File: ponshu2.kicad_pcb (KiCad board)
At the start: 2 copper layers, 22 parts, among them J1 Conn_01x02, J2 Conn_01x03, J3 Conn_01x05, SW1 TS-1187A-B-A-B, SW2 TS-1187A-B-A-B, U1 STM32F072CBT6, U2 XC6206P332MR

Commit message: sukoshi susumeta
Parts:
- added J4: Conn_01x02, Connector_PinHeader_2.54mm:PinHeader_1x02_P2.54mm_Vertical, F.Cu at (92.2, 89.4)
- added J5: Conn_01x03, Connector_PinHeader_2.54mm:PinHeader_1x03_P2.54mm_Vertical, F.Cu at (83.6, 91.2)
- ESD1, ESD2: footprint Diode_SMD:D_SOD-882 -> Diode_SMD:D_0402_1005Metric
- SW1, SW2: footprint random-keyboard-parts:SKQG-1155865 -> random-keyboard-parts:SKQGADE010
- U2: footprint Package_TO_SOT_SMD:SOT-23-3 -> Package_TO_SOT_SMD:SOT-23
- USB1: footprint Connector_USB:USB_C_Receptacle_HRO_TYPE-C-31-M-12 -> Type-C:HRO-TYPE-C-31-M-12-HandSoldering
- moved R2 24.6 mm to (69.3, 79.6), turned to -90 degrees
- moved J3 17.3 mm to (104.4, 70.6)
- moved R3 16.1 mm to (69.3, 74.0), turned to 90 degrees
- moved ESD1 2.62 mm to (70.9, 75.5), turned to -90 degrees
- moved ESD2 2.51 mm to (70.9, 78.0), turned to 90 degrees
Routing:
- net D+: track 0.00 -> 9.99 mm
- net Net-(F1-Pad1): track 0.00 -> 9.76 mm, vias 0 -> 2
- net GND: track 0.00 -> 8.76 mm
- net D-: track 0.00 -> 8.25 mm
- net Net-(USB1-CC1): track 0.00 -> 4.49 mm
- net Net-(USB1-CC2): track 0.00 -> 4.33 mm

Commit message: kiban susumeta
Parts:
- added J1: Conn_01x04, Connector_PinHeader_2.54mm:PinHeader_1x04_P2.54mm_Vertical, F.Cu at (82.9, 80.5)
- added J2: Conn_01x01, Connector_PinHeader_2.54mm:PinHeader_1x01_P2.54mm_Vertical, F.Cu at (75.7, 73.3)
- added J6: Conn_01x01, Connector_PinHeader_2.54mm:PinHeader_1x01_P2.54mm_Vertical, F.Cu at (75.7, 80.3)
- C1: renamed from C7; moved to B.Cu
- C2: renamed from C8; moved to B.Cu
- F1: moved to B.Cu
- J3: value Conn_01x05 -> Conn_01x01; footprint Connector_PinHeader_2.54mm:PinHeader_1x05_P2.54mm_Vertical -> Connector_PinHeader_2.54mm:PinHeader_1x01_P2.54mm_Vertical
- J4: value Conn_01x02 -> Conn_01x01; footprint Connector_PinHeader_2.54mm:PinHeader_1x02_P2.54mm_Vertical -> Connector_PinHeader_2.54mm:PinHeader_1x01_P2.54mm_Vertical
- J5: value Conn_01x03 -> Conn_01x01; footprint Connector_PinHeader_2.54mm:PinHeader_1x03_P2.54mm_Vertical -> Connector_PinHeader_2.54mm:PinHeader_1x01_P2.54mm_Vertical
- U1: renamed from U2; moved to B.Cu
- moved U2 39.8 mm to (94.5, 75.7), turned to 180 degrees
- moved C5 38.9 mm to (91.4, 69.3)
- moved SW2 38.6 mm to (82.5, 96.5)
- moved J3 33.3 mm to (72.5, 80.3)
- moved R3 32.9 mm to (106.6, 92.4)
- moved C8 29.5 mm to (88.1, 79.0), turned to 90 degrees
- moved C7 27.5 mm to (100.8, 74.5), turned to -90 degrees
- moved C3 22.9 mm to (80.8, 101.9)
- moved J4 21.5 mm to (75.7, 75.6)
- moved U1 19.9 mm to (72.5, 74.6), turned to 90 degrees
- moved SW1 19.7 mm to (100.0, 97.0)
- moved C6 18.2 mm to (97.6, 82.0), turned to 180 degrees
- moved J5 15.5 mm to (75.7, 77.9)
- moved C1 15.1 mm to (69.1, 73.8), turned to -90 degrees
- moved C4 14.4 mm to (100.8, 79.0), turned to -90 degrees
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- renumbered C6 to C3, C5 to C4, C4 to C5, C3 to C6, C2 to C7, C1 to C8, J1 to J7, J2 to J8, R2 to R1, R3 to R2, R1 to R3, SW2 to SW1, SW1 to SW2, U1 to U2
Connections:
- J3 pad 1: GND -> +3.3V
- J4 pad 1: +5v -> D-
- J5 pad 1: D- -> D+
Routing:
- net GND: track 8.76 -> 119.9 mm, vias 0 -> 6
- net +3.3V: track 0.00 -> 109.2 mm, vias 0 -> 8
- net D+: track 9.99 -> 31.5 mm
- net D-: track 8.25 -> 28.8 mm
- net +5v: track 0.00 -> 11.6 mm, vias 0 -> 1
- net Net-(F1-Pad1): track 9.76 -> 12.6 mm
- added copper zone on B.Cu, net GND
- added copper zone on F.Cu, net GND
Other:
- board outline added: 61.6 x 41.7 mm
- board text added: "+"
- board text added: "-"
- board text added: "3"
- board text added: "3V"
- board text added: "5V"
- board text added: "D+"
- board text added: "D-"
- board text added: "G"
- board text added: "GD"

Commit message: kiban susumetazo!
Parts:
- added J10: Conn_01x01, Connector_PinHeader_2.54mm:PinHeader_1x01_P2.54mm_Vertical, F.Cu at (92.1, 65.7)
- added J11: Conn_01x01, Connector_PinHeader_2.54mm:PinHeader_1x01_P2.54mm_Vertical, F.Cu at (91.2, 63.4)
- added J12: Conn_01x01, Connector_PinHeader_2.54mm:PinHeader_1x01_P2.54mm_Vertical, F.Cu at (89.5, 65.4)
- added J13: Conn_01x01, Connector_PinHeader_2.54mm:PinHeader_1x01_P2.54mm_Vertical, F.Cu at (91.6, 86.1)
- added J14: Conn_01x01, Connector_PinHeader_2.54mm:PinHeader_1x01_P2.54mm_Vertical, F.Cu at (93.0, 83.8)
- added J15: Conn_01x01, Connector_PinHeader_2.54mm:PinHeader_1x01_P2.54mm_Vertical, F.Cu at (93.9, 86.1)
- added J16: Conn_01x01, Connector_PinHeader_2.54mm:PinHeader_1x01_P2.54mm_Vertical, F.Cu at (95.6, 84.1)
- added J17: Conn_01x01, Connector_PinHeader_2.54mm:PinHeader_1x01_P2.54mm_Vertical, F.Cu at (96.3, 86.2)
- added J18: Conn_01x01, Connector_PinHeader_2.54mm:PinHeader_1x01_P2.54mm_Vertical, F.Cu at (98.2, 83.9)
- added J19: Conn_01x01, Connector_PinHeader_2.54mm:PinHeader_1x01_P2.54mm_Vertical, F.Cu at (99.4, 86.2)
- added J2: Conn_01x01, Connector_PinHeader_2.54mm:PinHeader_1x01_P2.54mm_Vertical, F.Cu at (82.9, 67.2)
- added J20: Conn_01x01, Connector_PinHeader_2.54mm:PinHeader_1x01_P2.54mm_Vertical, F.Cu at (88.5, 63.4)
- added J21: Conn_01x01, Connector_PinHeader_2.54mm:PinHeader_1x01_P2.54mm_Vertical, F.Cu at (87.1, 65.3)
- added J29: Conn_01x01, Connector_PinHeader_2.54mm:PinHeader_1x01_P2.54mm_Vertical, F.Cu at (97.8, 65.8)
- added J3: Conn_01x01, Connector_PinHeader_2.54mm:PinHeader_1x01_P2.54mm_Vertical, F.Cu at (81.5, 65.5)
- added J30: Conn_01x01, Connector_PinHeader_2.54mm:PinHeader_1x01_P2.54mm_Vertical, F.Cu at (96.5, 63.6)
- added J31: Conn_01x01, Connector_PinHeader_2.54mm:PinHeader_1x01_P2.54mm_Vertical, F.Cu at (95.0, 65.7)
- added J32: Conn_01x01, Connector_PinHeader_2.54mm:PinHeader_1x01_P2.54mm_Vertical, F.Cu at (93.7, 63.5)
- added J33: Conn_01x01, Connector_PinHeader_2.54mm:PinHeader_1x01_P2.54mm_Vertical, F.Cu at (90.4, 83.8)
- added J34: Conn_01x01, Connector_PinHeader_2.54mm:PinHeader_1x01_P2.54mm_Vertical, F.Cu at (79.4, 69.3)
- added J35: Conn_01x01, Connector_PinHeader_2.54mm:PinHeader_1x01_P2.54mm_Vertical, F.Cu at (82.2, 84.2)
- added J36: Conn_01x01, Connector_PinHeader_2.54mm:PinHeader_1x01_P2.54mm_Vertical, F.Cu at (84.8, 84.2)
- added J37: Conn_01x01, Connector_PinHeader_2.54mm:PinHeader_1x01_P2.54mm_Vertical, F.Cu at (80.0, 67.3)
- added J38: Conn_01x01, Connector_PinHeader_2.54mm:PinHeader_1x01_P2.54mm_Vertical, F.Cu at (82.2, 86.5)
- added J39: Conn_01x01, Connector_PinHeader_2.54mm:PinHeader_1x01_P2.54mm_Vertical, F.Cu at (81.4, 69.5)
- added J4: Conn_01x01, Connector_PinHeader_2.54mm:PinHeader_1x01_P2.54mm_Vertical, F.Cu at (87.4, 83.9)
- added J5: Conn_01x01, Connector_PinHeader_2.54mm:PinHeader_1x01_P2.54mm_Vertical, F.Cu at (83.8, 65.2)
- added J6: Conn_01x01, Connector_PinHeader_2.54mm:PinHeader_1x01_P2.54mm_Vertical, F.Cu at (89.2, 86.4)
- added J7: Conn_01x01, Connector_PinHeader_2.54mm:PinHeader_1x01_P2.54mm_Vertical, F.Cu at (86.9, 86.2)
- added J8: Conn_01x01, Connector_PinHeader_2.54mm:PinHeader_1x01_P2.54mm_Vertical, F.Cu at (79.1, 65.3)
- added J9: Conn_01x01, Connector_PinHeader_2.54mm:PinHeader_1x01_P2.54mm_Vertical, F.Cu at (84.5, 86.4)
- moved C3 32.3 mm to (106.8, 82.8)
- moved SW2 30.1 mm to (107.0, 78.9), turned to 180 degrees
- moved SW1 24.6 mm to (107.0, 73.3)
- moved R3 23.0 mm to (106.7, 69.3)
- moved J28 11.9 mm to (116.3, 70.4)
- moved J27 6.38 mm to (116.2, 60.5)
- moved C6 1.71 mm to (98.8, 80.9), turned to -90 degrees
- moved C8 1.35 mm to (89.1, 80.0), turned to 180 degrees
- renumbered J2 to J22, J3 to J23, J4 to J24, J5 to J25, J6 to J26, J7 to J27, J8 to J28
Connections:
- U2 pad 14: unconnected-(U2-PA4-Pad14) -> Net-(J29-Pin_1)
- U2 pad 15: unconnected-(U2-PA5-Pad15) -> Net-(J30-Pin_1)
- U2 pad 16: unconnected-(U2-PA6-Pad16) -> Net-(J31-Pin_1)
- U2 pad 17: unconnected-(U2-PA7-Pad17) -> Net-(J32-Pin_1)
- U2 pad 18: unconnected-(U2-PB0-Pad18) -> Net-(J10-Pin_1)
- U2 pad 19: unconnected-(U2-PB1-Pad19) -> Net-(J11-Pin_1)
- U2 pad 20: unconnected-(U2-PB2-Pad20) -> Net-(J12-Pin_1)
- U2 pad 21: unconnected-(U2-PB10-Pad21) -> Net-(J20-Pin_1)
- U2 pad 22: unconnected-(U2-PB11-Pad22) -> Net-(J21-Pin_1)
- U2 pad 25: unconnected-(U2-PB12-Pad25) -> Net-(J5-Pin_1)
- U2 pad 26: unconnected-(U2-PB13-Pad26) -> Net-(J2-Pin_1)
- U2 pad 27: unconnected-(U2-PB14-Pad27) -> Net-(J3-Pin_1)
- U2 pad 28: unconnected-(U2-PB15-Pad28) -> Net-(J8-Pin_1)
- U2 pad 29: unconnected-(U2-PA8-Pad29) -> Net-(J36-Pin_1)
- U2 pad 30: unconnected-(U2-PA9-Pad30) -> Net-(J38-Pin_1)
- U2 pad 31: unconnected-(U2-PA10-Pad31) -> Net-(J34-Pin_1)
- U2 pad 38: unconnected-(U2-PA15-Pad38) -> Net-(J33-Pin_1)
- U2 pad 39: unconnected-(U2-PB3-Pad39) -> Net-(J13-Pin_1)
- U2 pad 40: unconnected-(U2-PB4-Pad40) -> Net-(J14-Pin_1)
- U2 pad 41: unconnected-(U2-PB5-Pad41) -> Net-(J15-Pin_1)
- U2 pad 42: unconnected-(U2-PB6-Pad42) -> Net-(J16-Pin_1)
- U2 pad 43: unconnected-(U2-PB7-Pad43) -> Net-(J17-Pin_1)
- U2 pad 45: unconnected-(U2-PB8-Pad45) -> Net-(J18-Pin_1)
- U2 pad 46: unconnected-(U2-PB9-Pad46) -> Net-(J19-Pin_1)
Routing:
- net SWDIO: track 0.00 -> 38.8 mm, vias 0 -> 2
- net Net-(U2-BOOT0): track 0.00 -> 32.9 mm, vias 0 -> 2
- net Net-(J2-Pin_1): track 0.00 -> 20.3 mm, vias 0 -> 2
- net Net-(J8-Pin_1): track 0.00 -> 19.5 mm, vias 0 -> 2
- net Net-(J38-Pin_1): track 0.00 -> 19.0 mm, vias 0 -> 2
- net NRST: track 0.00 -> 17.9 mm
- net Net-(J5-Pin_1): track 0.00 -> 17.7 mm, vias 0 -> 2
- net Net-(J3-Pin_1): track 0.00 -> 16.8 mm, vias 0 -> 2
- net Net-(J34-Pin_1): track 0.00 -> 16.0 mm, vias 0 -> 2
- net Net-(J36-Pin_1): track 0.00 -> 15.5 mm, vias 0 -> 2
- net SWCLK: track 0.00 -> 15.1 mm, vias 0 -> 1
- net GND: track 119.9 -> 134.6 mm, vias 6 -> 7
- net +3.3V: track 109.2 -> 119.1 mm
- net Net-(J19-Pin_1): track 0.00 -> 8.38 mm
- net Net-(J17-Pin_1): track 0.00 -> 8.32 mm, vias 0 -> 1
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- removed copper zone on B.Cu, net GND

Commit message: kiban no ana kankaku hiroku shita
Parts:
- added H1: MountingHole, MountingHole:MountingHole_2.5mm, F.Cu at (77.1, 67.3)
- added H2: MountingHole, MountingHole:MountingHole_2.5mm, F.Cu at (113.4, 67.2)
- added H3: MountingHole, MountingHole:MountingHole_2.5mm, F.Cu at (76.8, 85.1)
- added H4: MountingHole, MountingHole:MountingHole_2.5mm, F.Cu at (113.3, 84.8)
- moved J27 48.4 mm to (68.6, 69.1), turned to 90 degrees
- moved J30 11.6 mm to (107.4, 67.4)
- moved J29 11.6 mm to (109.3, 65.7)
- moved J31 10.7 mm to (105.7, 65.8)
- moved J32 10.5 mm to (103.5, 67.4)
- moved J10 9.91 mm to (102.0, 65.7)
- moved J11 9.72 mm to (100.1, 67.3)
- moved J12 8.77 mm to (98.3, 65.8)
- moved J28 8.57 mm to (114.0, 78.6), turned to 180 degrees
- moved J5 7.98 mm to (91.6, 67.1)
- moved J20 7.83 mm to (96.0, 65.7)
- moved J8 7.25 mm to (86.4, 65.7)
- moved J3 6.91 mm to (88.1, 67.6)
- moved J2 6.90 mm to (89.7, 65.7)
- moved J21 6.36 mm to (93.5, 65.7)
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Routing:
- net Net-(J29-Pin_1): track 1.76 -> 18.3 mm, vias 0 -> 1
- net Net-(J30-Pin_1): track 1.91 -> 14.7 mm, vias 0 -> 1
- net Net-(J31-Pin_1): track 1.91 -> 14.2 mm
- net GND: track 134.6 -> 145.2 mm
- net Net-(J38-Pin_1): track 19.0 -> 29.4 mm
- net Net-(J10-Pin_1): track 2.69 -> 12.4 mm, vias 0 -> 1
- net Net-(J32-Pin_1): track 2.05 -> 11.6 mm
- net Net-(J34-Pin_1): track 16.0 -> 25.3 mm
- net Net-(J8-Pin_1): track 19.5 -> 27.5 mm
- net Net-(J36-Pin_1): track 15.5 -> 23.3 mm
- net +3.3V: track 119.1 -> 126.2 mm
- net Net-(J11-Pin_1): track 2.69 -> 9.24 mm
- net Net-(J12-Pin_1): track 2.68 -> 8.82 mm
- net Net-(J2-Pin_1): track 20.3 -> 26.4 mm
- net Net-(J5-Pin_1): track 17.7 -> 23.4 mm
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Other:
- board size 61.6 x 41.7 mm -> 63.5 x 24.4 mm

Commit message: kiban hobo kansei shita
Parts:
- added REF**: MountingHole_2.1mm, MountingHole:MountingHole_2.1mm, F.Cu at (73.5, 81.5)
- added REF**: MountingHole_2.1mm, MountingHole:MountingHole_2.1mm, F.Cu at (73.5, 71.8)
- added REF**: MountingHole_2.1mm, MountingHole:MountingHole_2.1mm, F.Cu at (73.5, 77.5)
- added REF**: MountingHole_2.1mm, MountingHole:MountingHole_2.1mm, F.Cu at (73.5, 74.2)
- added REF**: MountingHole_2.1mm, MountingHole:MountingHole_2.1mm, F.Cu at (73.5, 75.8)
- added REF**: MountingHole_2.1mm, MountingHole:MountingHole_2.1mm, F.Cu at (73.5, 79.2)
- added REF**: MountingHole_2.1mm, MountingHole:MountingHole_2.1mm, F.Cu at (73.5, 74.9)
- added REF**: MountingHole_2.1mm, MountingHole:MountingHole_2.1mm, F.Cu at (73.5, 78.4)
- added REF**: MountingHole_2.1mm, MountingHole:MountingHole_2.1mm, F.Cu at (73.5, 80.3)
- added REF**: MountingHole_2.1mm, MountingHole:MountingHole_2.1mm, F.Cu at (73.5, 73.4)
- added REF**: MountingHole_2.1mm, MountingHole:MountingHole_2.1mm, F.Cu at (73.5, 72.8)
- moved J27 10.1 mm to (77.1, 74.5), turned to 180 degrees
- moved J19 9.92 mm to (109.3, 86.7)
- moved J17 9.79 mm to (106.0, 86.7)
- moved J18 9.56 mm to (107.7, 84.7)
- moved J16 8.19 mm to (103.8, 85.1)
- moved J15 8.16 mm to (102.0, 86.9)
- moved J14 7.15 mm to (99.9, 85.3)
- moved J13 6.79 mm to (98.3, 87.0)
- moved J33 6.25 mm to (95.9, 86.9)
- moved J7 2.71 mm to (89.5, 86.7)
- moved J6 2.56 mm to (91.4, 85.2)
- moved J9 1.97 mm to (86.4, 86.9)
- moved J4 1.27 mm to (88.1, 85.0)
- moved J38 1.09 mm to (83.2, 86.9)
- moved J36 0.65 mm to (84.7, 84.8)
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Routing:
- net SWDIO: track 39.1 -> 67.4 mm, vias 2 -> 4
- net SWCLK: track 13.0 -> 29.4 mm, vias 1 -> 2
- net GND: track 145.2 -> 160.0 mm, vias 7 -> 9
- net D+: track 36.8 -> 24.3 mm
- net D-: track 34.0 -> 21.5 mm
- net Net-(J19-Pin_1): track 8.38 -> 19.7 mm, vias 0 -> 1
- net Net-(J18-Pin_1): track 5.11 -> 14.9 mm
- net Net-(J16-Pin_1): track 4.95 -> 14.3 mm
- net Net-(J17-Pin_1): track 8.32 -> 17.5 mm
- net Net-(J15-Pin_1): track 6.61 -> 14.0 mm
- net Net-(J14-Pin_1): track 4.08 -> 11.2 mm
- net Net-(J33-Pin_1): track 4.72 -> 9.45 mm
- net NRST: track 17.9 -> 22.5 mm
- net Net-(J13-Pin_1): track 6.74 -> 11.3 mm
- net Net-(J3-Pin_1): track 21.6 -> 24.4 mm, vias 3 -> 2
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- added copper zone on B.Cu, net GND
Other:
- outline, holes or cut-outs redrawn
- board text added: "CL"
- board text added: "DIO"
- board text added: "GND"
- board text added: "NRST"
- board text added: "lc0"
- board text added: "lc7"
- board text added: "r0"
- board text added: "r6"
- board text added: "rc0"
- board text added: "rc8"
- board text removed: "+"
- board text removed: "-"
- board text removed: "3"
- board text removed: "G"
- board text removed: "GD"

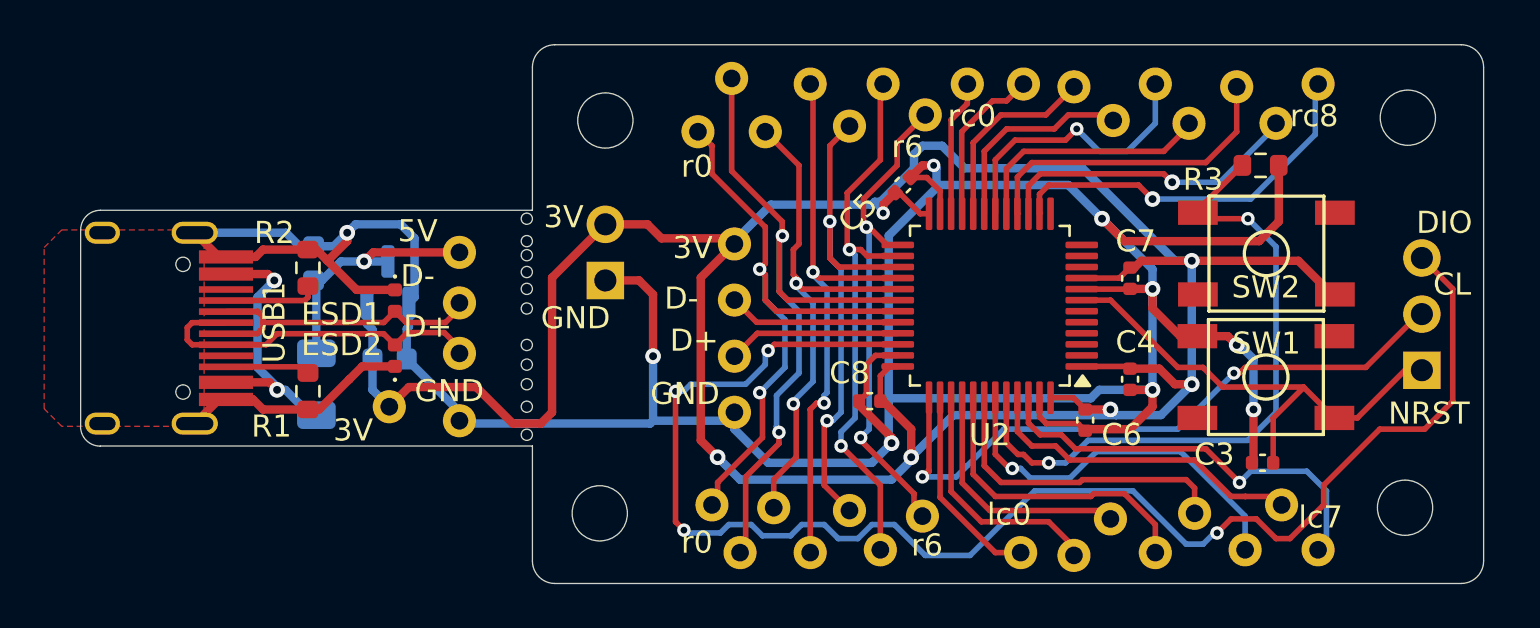
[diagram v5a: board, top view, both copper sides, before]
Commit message: kiban kansei
names of kiban are Piece1 and Piece2
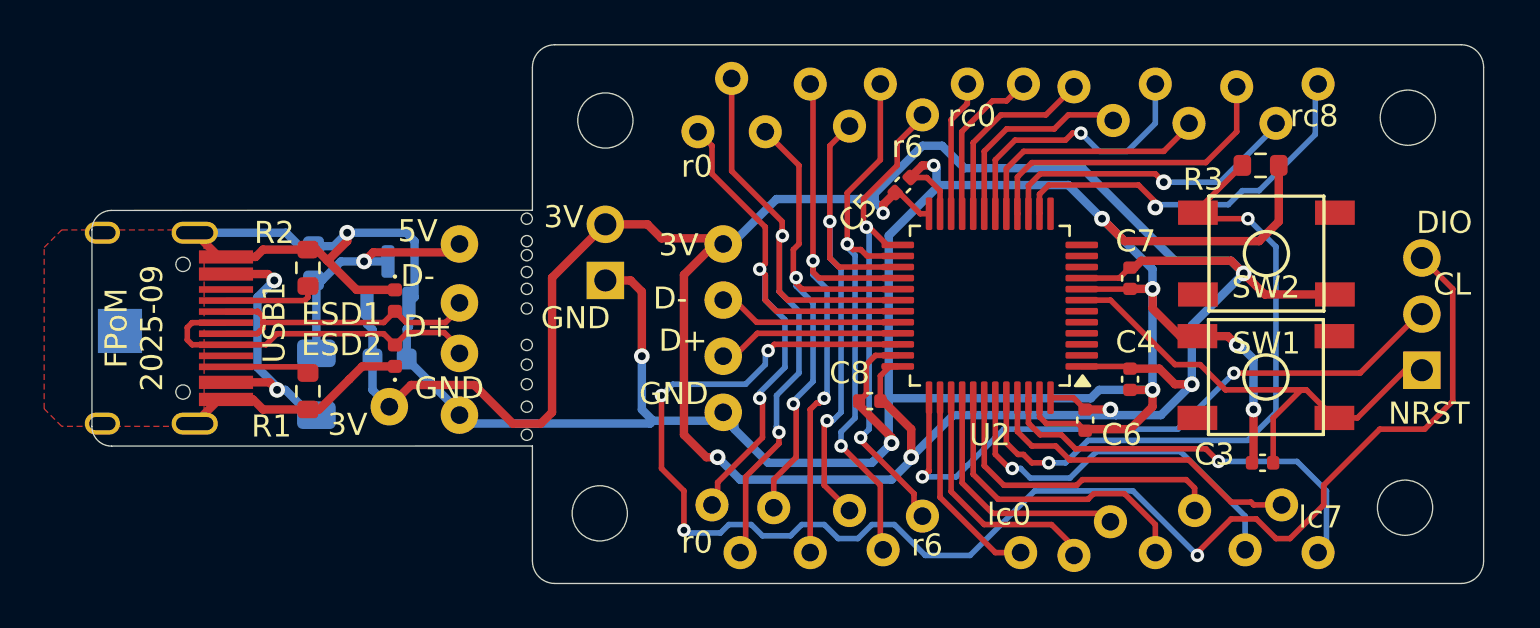
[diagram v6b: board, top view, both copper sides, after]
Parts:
- added REF**: SolderWirePad_1x01_SMD_1x2mm, Connector_Wire:SolderWirePad_1x01_SMD_1x2mm, B.Cu at (55.1, 76.8)
- moved J1 0.51 mm to (82.4, 80.5)
- moved J22 0.38 mm to (70.5, 72.9)
- moved J26 0.25 mm to (70.5, 80.6)
- moved J14 0.13 mm to (99.9, 85.5)
- moved J16 0.13 mm to (103.8, 85.0)
- moved J2 0.13 mm to (89.5, 65.7)
- moved J7 0.13 mm to (89.7, 86.7)
- moved J19 0.13 mm to (109.3, 86.9)
- moved J5 0.13 mm to (91.4, 67.1)
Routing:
- net +3.3V: track 126.0 -> 129.8 mm
- net SWDIO: track 67.4 -> 68.7 mm
- net D+: track 24.3 -> 25.2 mm
- net GND: track 160.0 -> 159.4 mm
- net D-: track 21.5 -> 22.0 mm
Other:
- board size 63.5 x 24.4 mm -> 63 x 24.4 mm
- board text added: "FPoM 2025-09"
- board text added: "First Product of Murahana 2025-09"
- board text added: "Piece1"
- board text added: "Piece2"
- board text added: "t-miyajima"
